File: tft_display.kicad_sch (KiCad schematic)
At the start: 7 parts, among them J4 Conn_01x04_Socket, J6 Conn_01x08_Socket, J8 Conn_01x06_Socket

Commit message: Fix ERC errors.
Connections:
- net LCD_GND is gone; now on net GND: DS1.B2 (GND), J6.6 (Pin_6)
- net LCD_VCC renamed +3V3
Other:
- moved on the sheet: R13, R18, R19

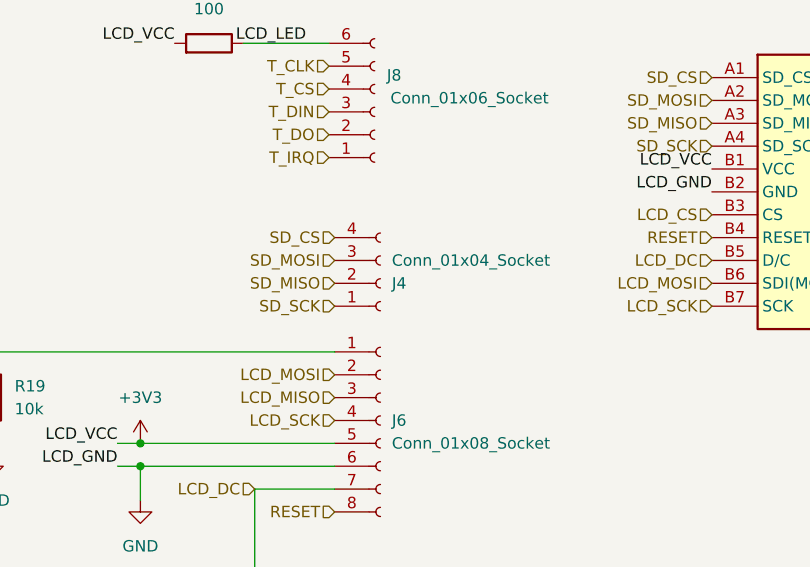
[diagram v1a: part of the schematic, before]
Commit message: Remove duplicated power flag.
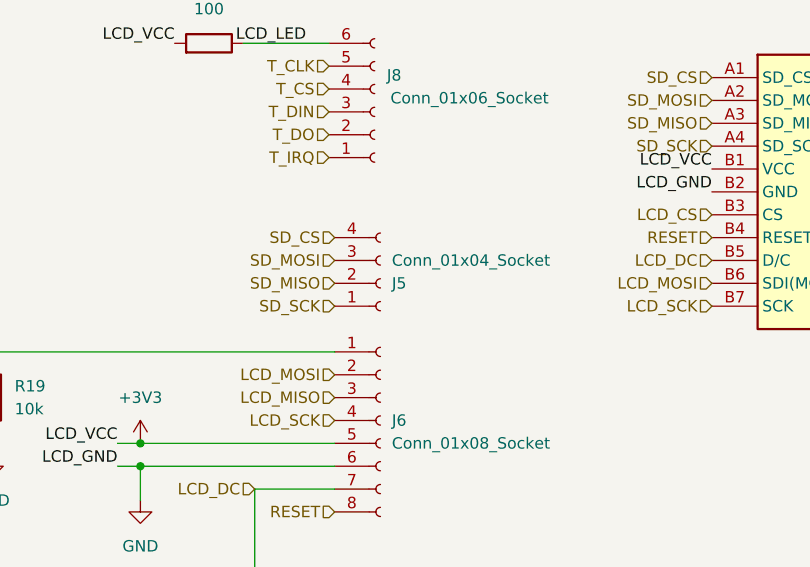
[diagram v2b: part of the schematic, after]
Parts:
- renumbered J4 to J5
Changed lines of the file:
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@@
 		(in_pos_files yes)
 		(dnp no)
-		(property "Reference" "J4"
+		(property "Reference" "J5"
 			(at 107.95 92.7101 0)
 			(show_name no)
@@
 			(project "CC3501-project-hardware"
 				(path "/4a2d49bb-8ba4-4c60-a8f0-05b8d2544445/50ab5461-2300-442b-bf4b-f1a79527a3c6"
-					(reference "J4")
+					(reference "J5")
 					(unit 1)
 				)

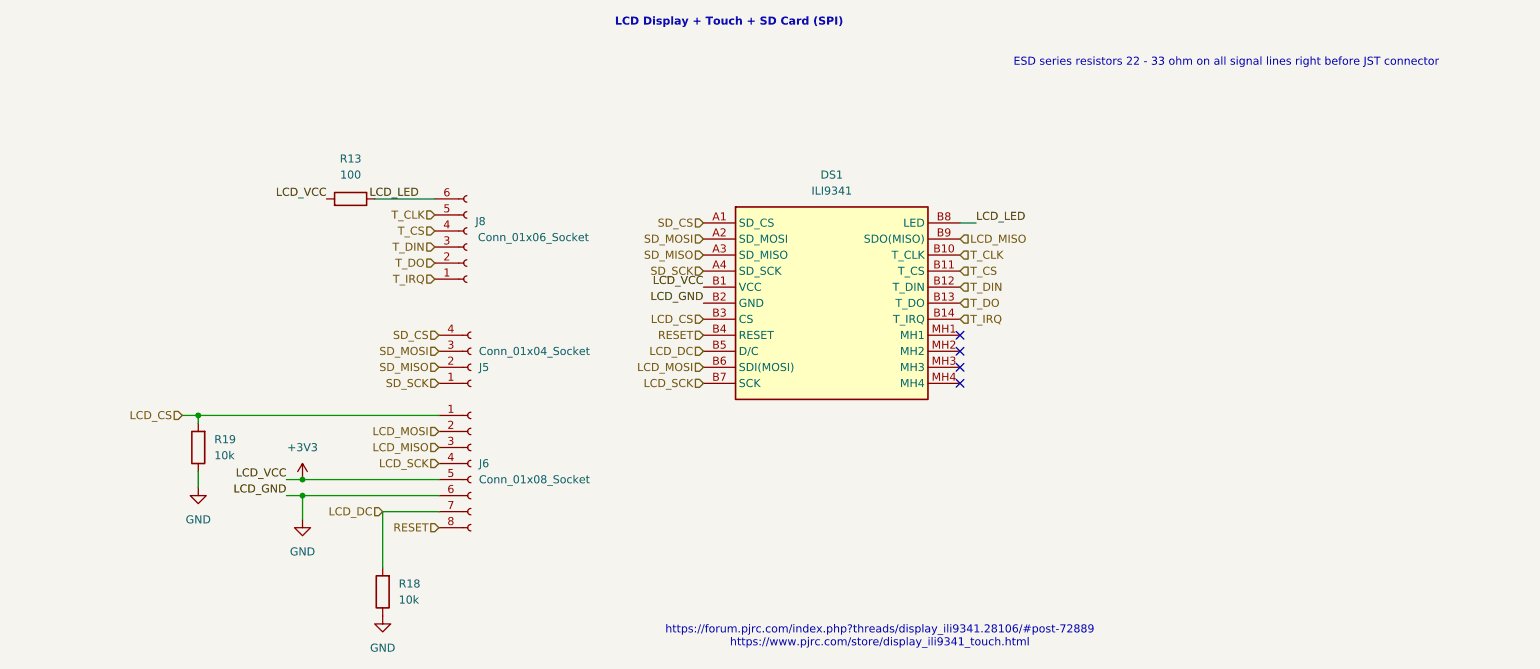
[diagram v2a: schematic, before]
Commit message: Rewire TFT display to power with 5V and allowing backlight switching via FET.
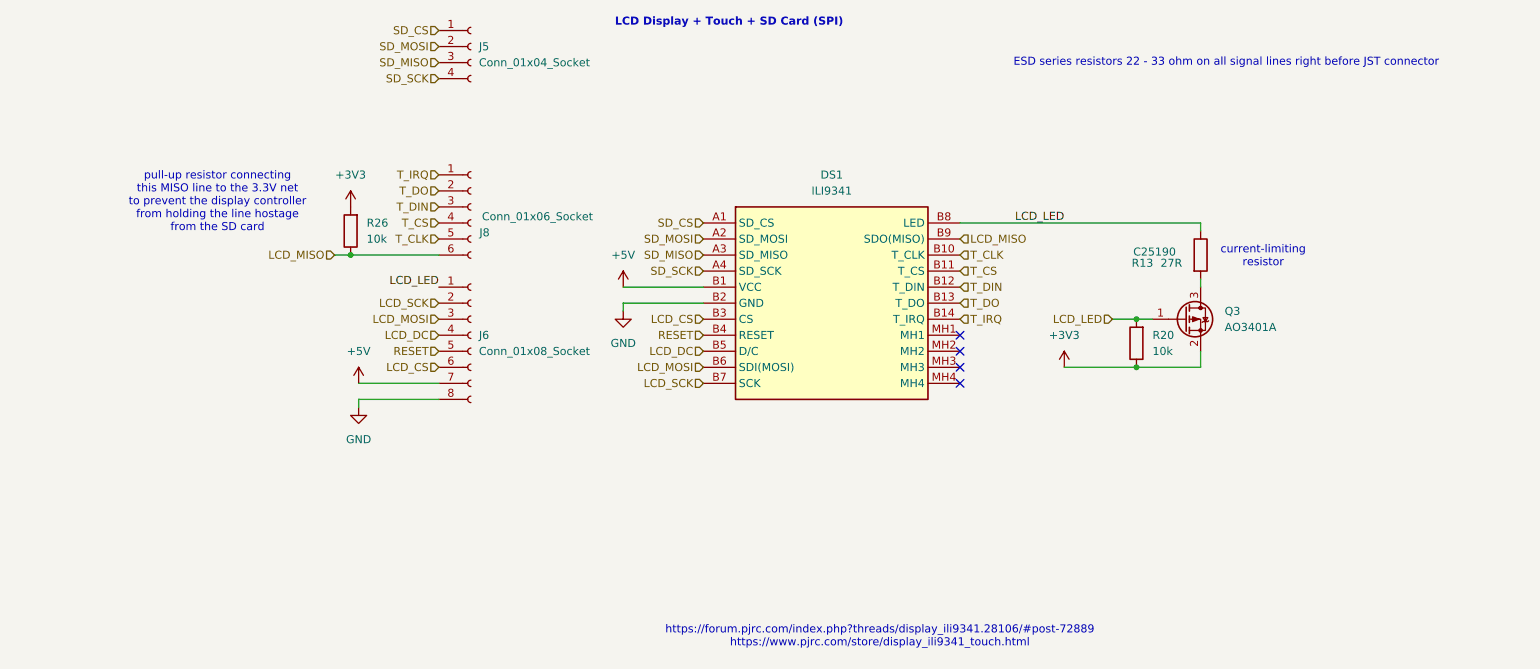
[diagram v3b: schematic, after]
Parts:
- removed R18, R19: 10k, Resistor_SMD:R_0805_2012Metric, symbol Device:R
- added Q3: AO3401A, Package_TO_SOT_SMD:SOT-23, symbol Transistor_FET:AO3401A
- added R20, R26: 10k, Resistor_SMD:R_0805_2012Metric, symbol Device:R
- R13: value 100 -> 27R; footprint Resistor_SMD:R_0402_1005Metric -> Resistor_SMD:R_0201_0603Metric; LCSC PN C25076 -> C25190
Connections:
- net +3V3: now also Q3.2 (S), R20.1, R26.2; no longer DS1.B1 (VCC), J6.5 (Pin_5), R13.2
- net GND: now also J6.8 (Pin_8); no longer J6.6 (Pin_6)
- net LCD_CS: now also J6.6 (Pin_6); no longer J6.1 (Pin_1)
- net LCD_DC: now also J6.4 (Pin_4); no longer J6.7 (Pin_7)
- net LCD_LED: now also J6.1 (Pin_1), Q3.1 (G), R20.2; no longer J8.6 (Pin_6)
- net LCD_MISO: now also J8.6 (Pin_6), R26.1; no longer J6.3 (Pin_3)
- net LCD_MOSI: now also J6.3 (Pin_3); no longer J6.2 (Pin_2)
- net LCD_SCK: now also J6.2 (Pin_2); no longer J6.4 (Pin_4)
- net RESET: now also J6.5 (Pin_5); no longer J6.8 (Pin_8)
- net SD_CS: now also J5.1 (Pin_1); no longer J5.4 (Pin_4)
- net SD_MISO: now also J5.3 (Pin_3); no longer J5.2 (Pin_2)
- net SD_MOSI: now also J5.2 (Pin_2); no longer J5.3 (Pin_3)
- net SD_SCK: now also J5.4 (Pin_4); no longer J5.1 (Pin_1)
- new net: Q3.3 (D), R13.2
- new net +5V: DS1.B1 (VCC), J6.7 (Pin_7)
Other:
- note added: "current-limiting resistor"
- note added: "pull-up resistor connecting this MISO line to the 3.3V net to prevent the display controller from holding the line hostage from the SD card"
- moved on the sheet: J5, J6, J8

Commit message: edit HX711 configuration to match datasheet and sparkfun example as well as add JLC part numbers and display them on schematic
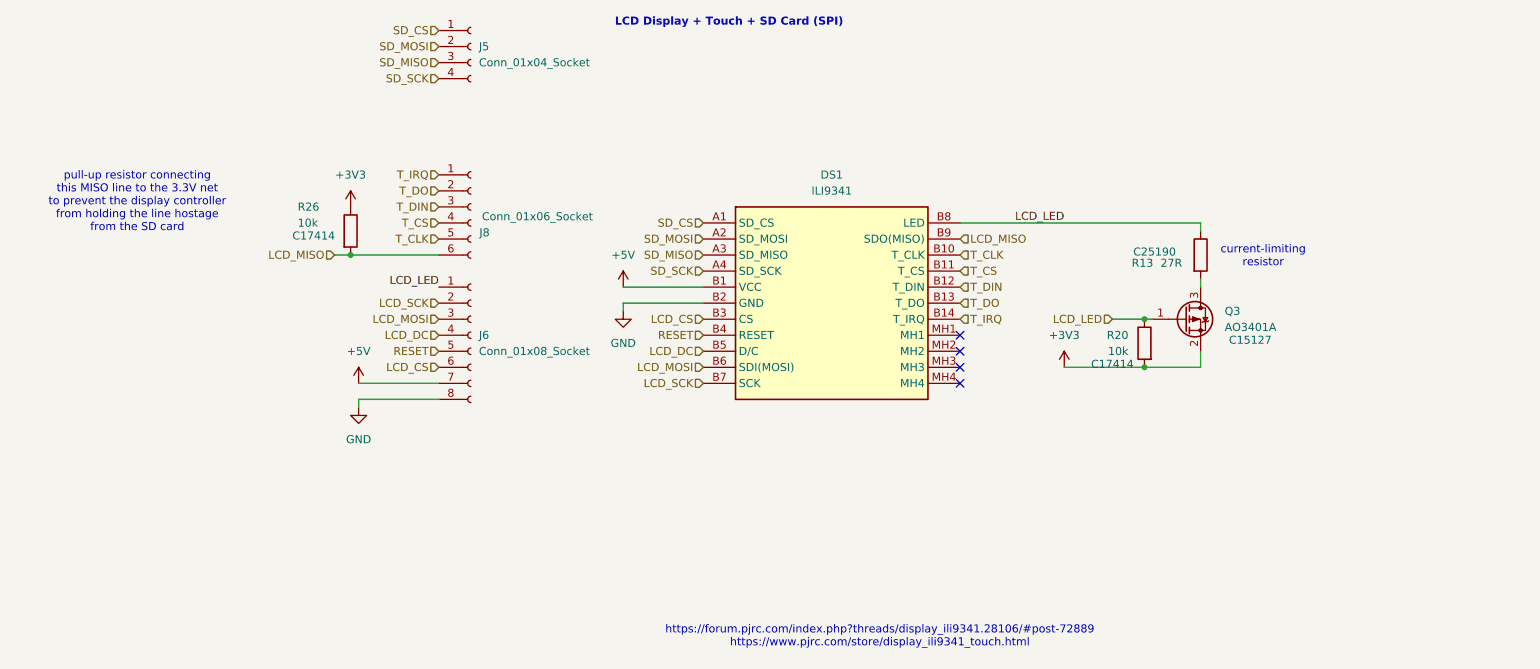
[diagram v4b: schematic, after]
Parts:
- J5: footprint (none) -> Connector_PinHeader_2.54mm:PinHeader_1x04_P2.54mm_Vertical
- J6: footprint (none) -> Connector_PinHeader_2.54mm:PinHeader_1x08_P2.54mm_Vertical
- J8: footprint (none) -> Connector_PinHeader_2.54mm:PinHeader_1x06_P2.54mm_Vertical
- Q3: LCSC PN (none) -> C15127
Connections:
- net +3V3: now also R20.2, R26.1; no longer R20.1, R26.2
- net LCD_LED: now also R20.1; no longer R20.2
- net LCD_MISO: now also R26.2; no longer R26.1
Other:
- note removed: "ESD series resistors 22 - 33 ohm on all signal lines right before JST connector"
